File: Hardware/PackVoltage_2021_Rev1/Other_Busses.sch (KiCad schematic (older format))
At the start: 50 parts, among them Q5 Q_NMOS_DGS, Q6 Q_NMOS_DGS, Q7 Q_NMOS_DGS, Q8 Q_NMOS_DGS, U13 LT1910, U14 LT1910, U15 LT1910, U16 INA281, U17 INA281, U18 INA281, U19 LT1910, U20 INA281, U21 LT1910, U22 INA281

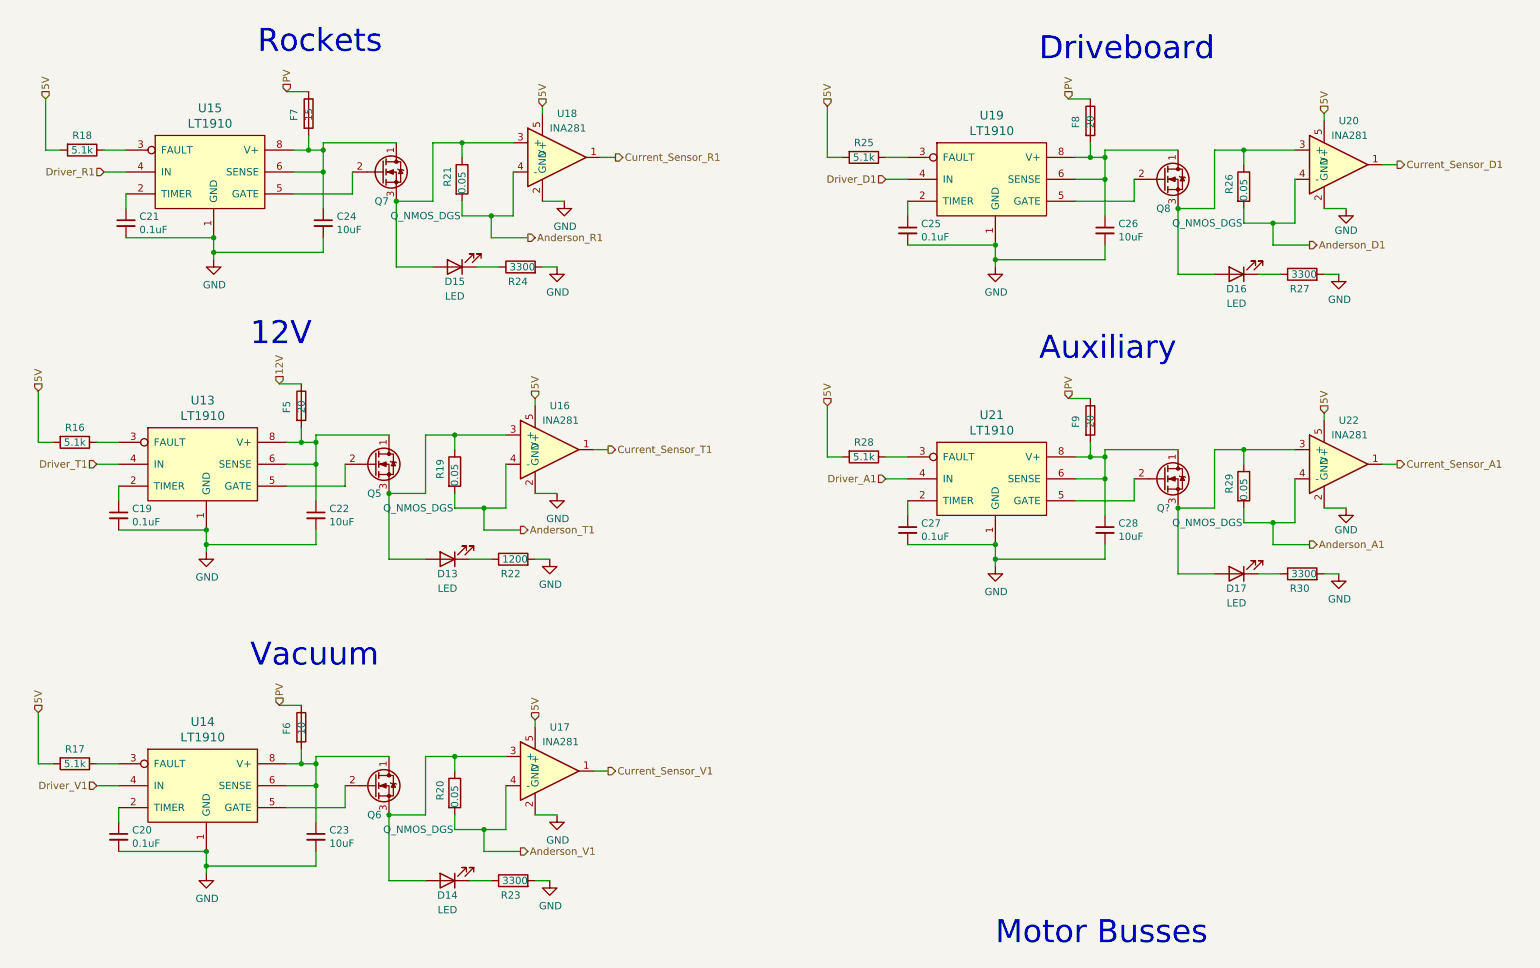
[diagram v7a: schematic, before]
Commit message: Added GimbalSense, reannotated
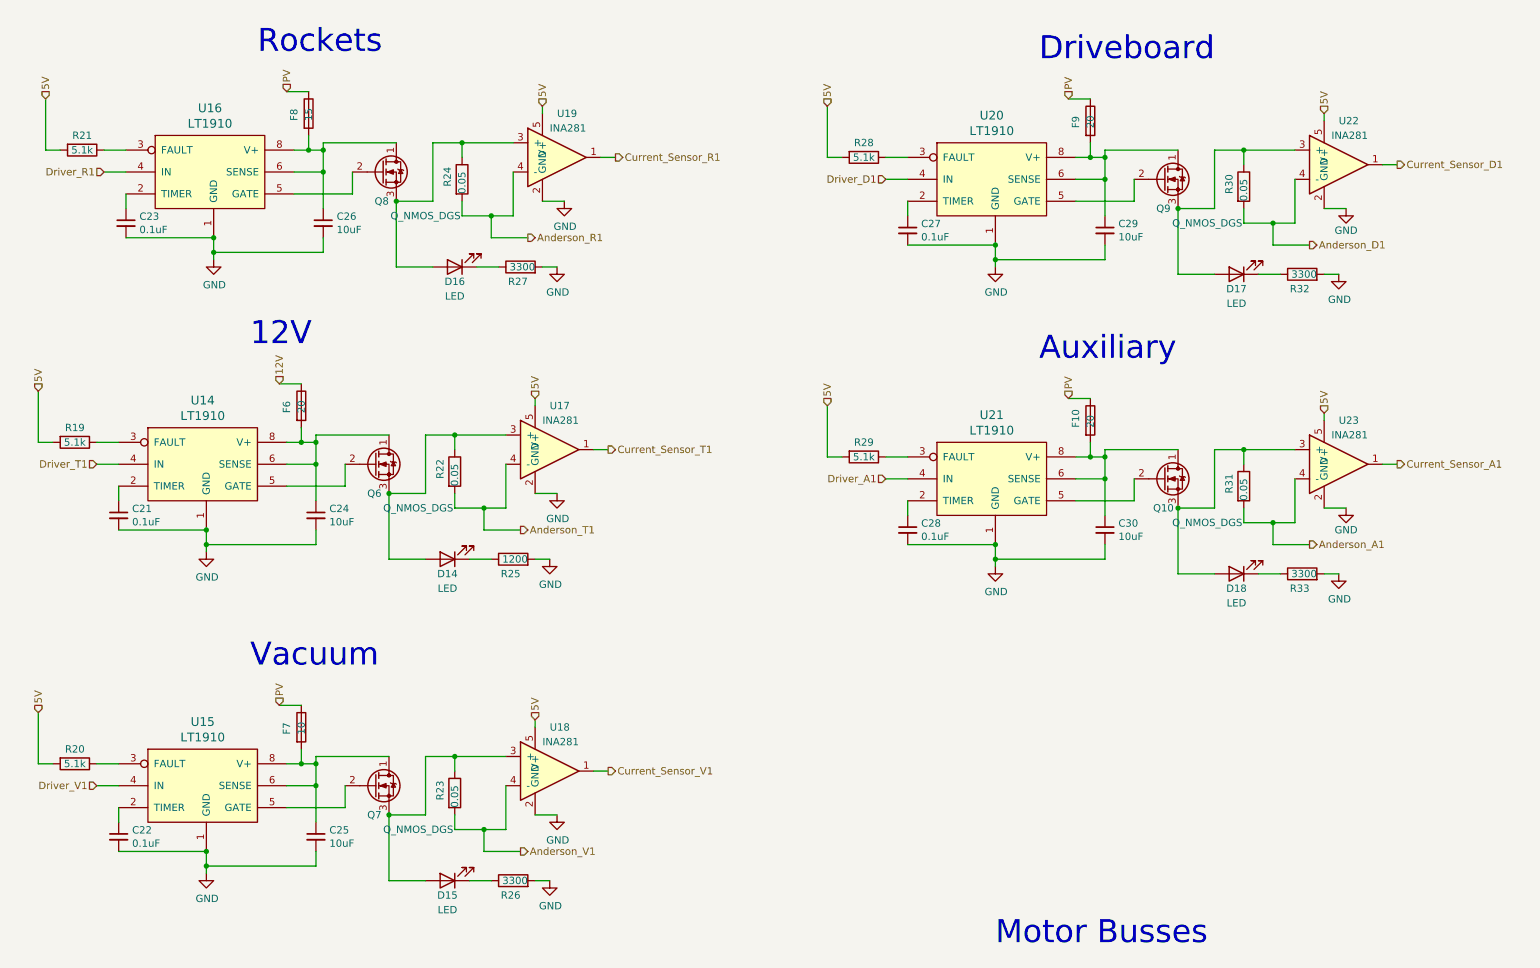
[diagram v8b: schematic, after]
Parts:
- gave numbers to parts that had none: 1
- renumbered C19 to C21, C20 to C22, C21 to C23, C22 to C24, C23 to C25, C24 to C26, C25 to C27, C27 to C28, C26 to C29, C28 to C30, D13 to D14, D14 to D15, D15 to D16, D16 to D17, D17 to D18, F9 to F10, F5 to F6, F6 to F7, F7 to F8, F8 to F9, Q5 to Q6, Q6 to Q7, Q7 to Q8, Q8 to Q9, R16 to R19, R17 to R20, R18 to R21, R19 to R22, R20 to R23, R21 to R24, R22 to R25, R23 to R26, R24 to R27, R25 to R28, R28 to R29, R26 to R30, R29 to R31, R27 to R32, R30 to R33, U13 to U14, U14 to U15, U15 to U16, U16 to U17, U17 to U18, U18 to U19, U19 to U20, U20 to U22, U22 to U23
